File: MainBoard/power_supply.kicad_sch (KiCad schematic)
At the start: 17 parts, among them J10 1761681-3

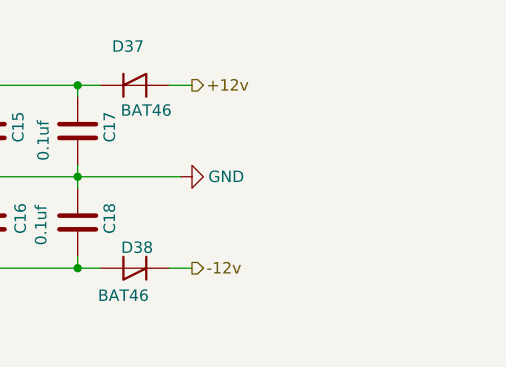
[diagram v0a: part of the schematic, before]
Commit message: added additional voltage source for simulation
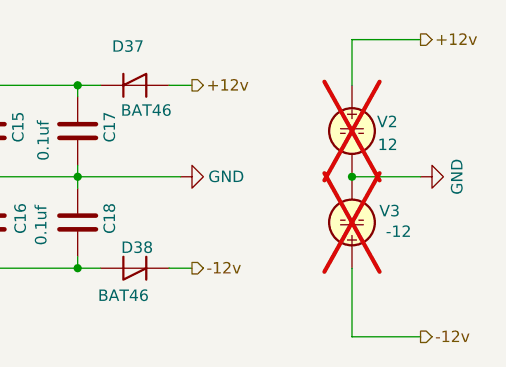
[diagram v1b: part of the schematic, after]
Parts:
- added V2: 12, symbol Simulation_SPICE:VDC
- added V3: -12, symbol Simulation_SPICE:VDC
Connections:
- net +12v: now also V2.1
- net -12v: now also V3.1
- net GND: now also V2.2, V3.2

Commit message: WIP: trying to figure out connection issues
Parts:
- removed V2: 12, symbol Simulation_SPICE:VDC
- removed V3: -12, symbol Simulation_SPICE:VDC
- D35: footprint Diode_THT:D_DO-35_SOD27_P7.62mm_Horizontal -> Diode_THT:D_DO-201_P12.70mm_Horizontal
- D36: footprint Diode_THT:D_DO-35_SOD27_P7.62mm_Horizontal -> Diode_THT:D_DO-201_P15.24mm_Horizontal
- renumbered V4 to V1, V6 to V2
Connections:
- net +12v renamed +v
- net -12v renamed -v
